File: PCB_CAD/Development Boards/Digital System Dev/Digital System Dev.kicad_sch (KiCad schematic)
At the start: 73 parts, among them J1 STLINK, J10 10V, J2 PINS_LEFT, J3 3V3, J4 5V, J5 GND, J6 PINS_LEFT, J7 DISP, J9 DC_IN, SW1 RESET, U1 STM32G474VETx, U2 DFR0570, U3 DFR0571, X1 HSE_24

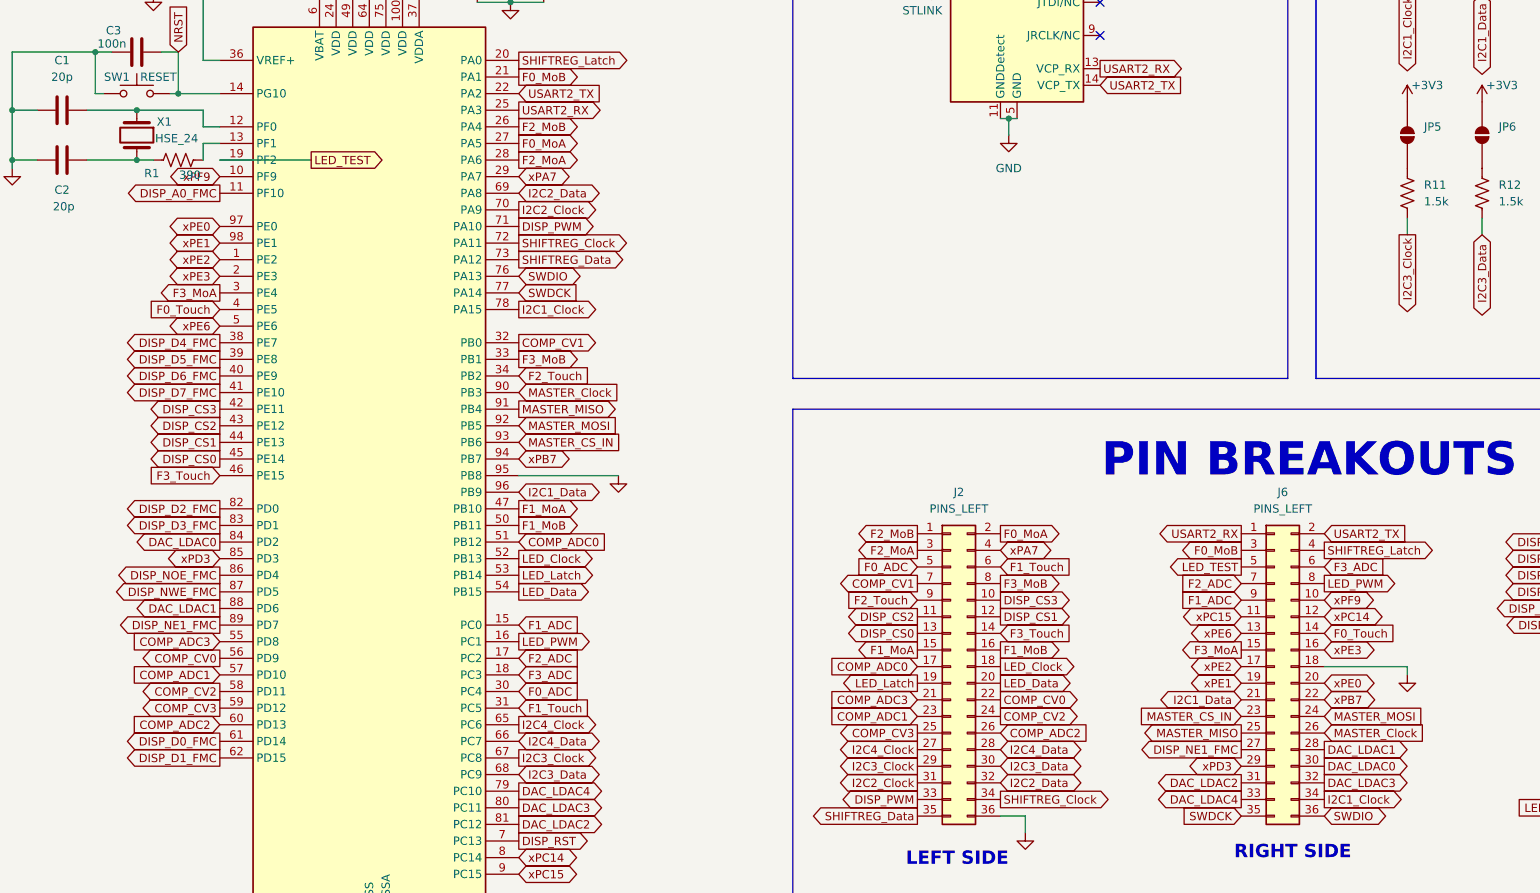
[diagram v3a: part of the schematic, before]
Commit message: fixed led flickering bug due to waiting for floating disconnnected i2c buses to respond until timeout
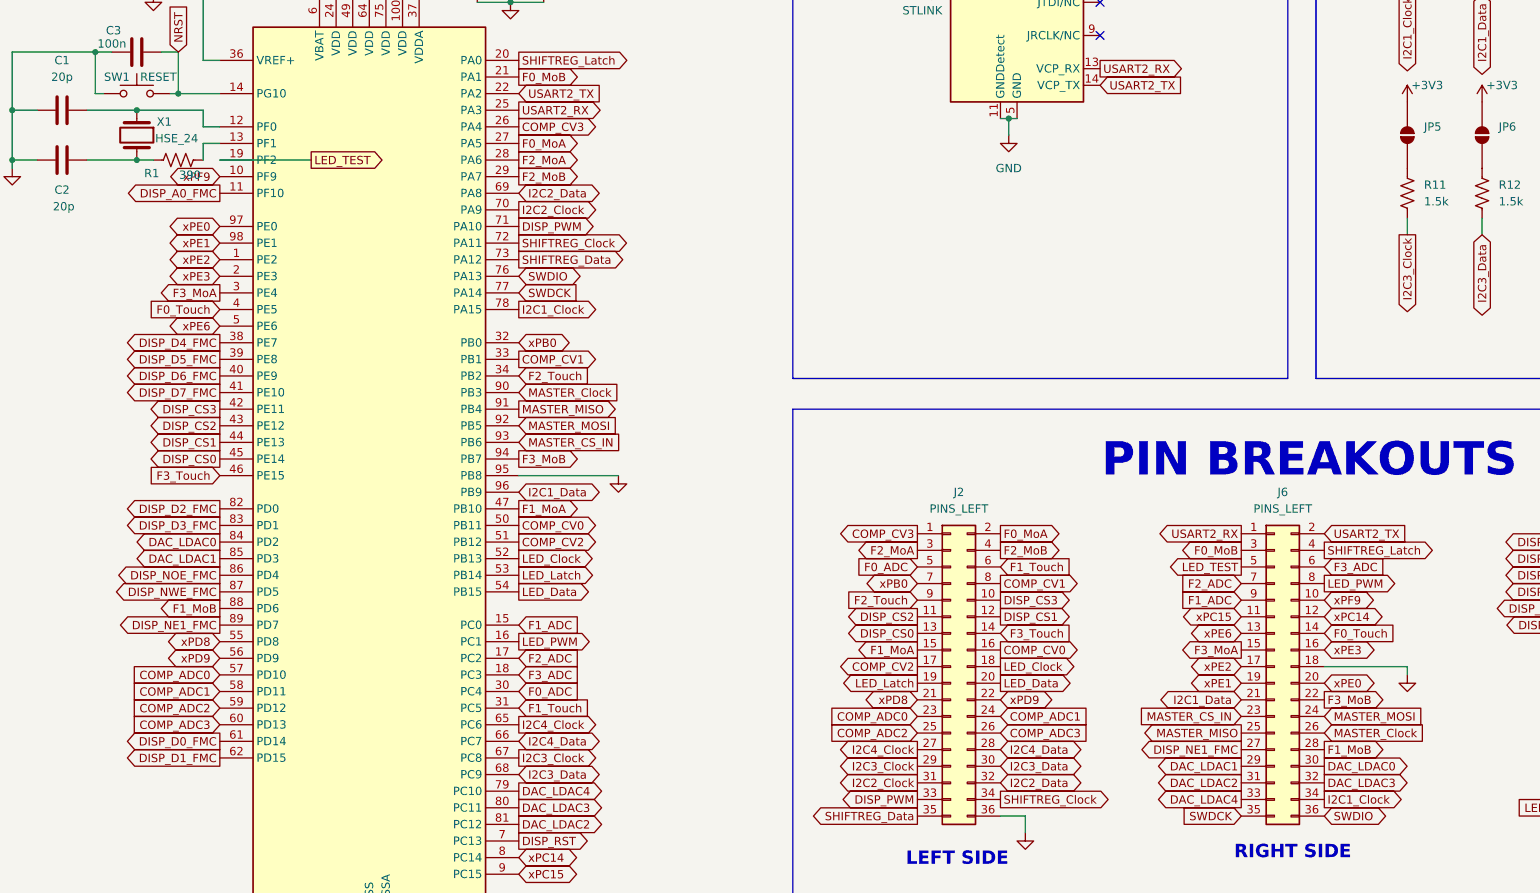
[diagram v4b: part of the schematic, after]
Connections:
- net xPA7 is gone; now on net F2_MoB: J2.4 (Pin_4), U1.29 (PA7)
- net xPB7 is gone; now on net F3_MoB: J6.22 (Pin_22), U1.94 (PB7)
- net xPD3 is gone; now on net DAC_LDAC1: J6.29 (Pin_29), U1.85 (PD3)
- net COMP_ADC0: now also J2.23 (Pin_23), U1.57 (PD10); no longer J2.17 (Pin_17), U1.51 (PB12)
- net COMP_ADC1: now also J2.24 (Pin_24), U1.58 (PD11); no longer J2.23 (Pin_23), U1.57 (PD10)
- net COMP_ADC2: now also J2.25 (Pin_25), U1.59 (PD12); no longer J2.26 (Pin_26), U1.60 (PD13)
- net COMP_ADC3: now also J2.26 (Pin_26), U1.60 (PD13); no longer J2.21 (Pin_21), U1.55 (PD8)
- net COMP_CV0: now also J2.16 (Pin_16), U1.50 (PB11); no longer J2.22 (Pin_22), U1.56 (PD9)
- net COMP_CV1: now also J2.8 (Pin_8), U1.33 (PB1); no longer J2.7 (Pin_7), U1.32 (PB0)
- net COMP_CV2: now also J2.17 (Pin_17), U1.51 (PB12); no longer J2.24 (Pin_24), U1.58 (PD11)
- net COMP_CV3: now also J2.1 (Pin_1), U1.26 (PA4); no longer J2.25 (Pin_25), U1.59 (PD12)
- net DAC_LDAC1: no longer J6.28 (Pin_28), U1.88 (PD6)
- net F1_MoB: now also J6.28 (Pin_28), U1.88 (PD6); no longer J2.16 (Pin_16), U1.50 (PB11)
- net F2_MoB: no longer J2.1 (Pin_1), U1.26 (PA4)
- net F3_MoB: no longer J2.8 (Pin_8), U1.33 (PB1)
- new net xPB0: J2.7 (Pin_7), U1.32 (PB0)
- new net xPD8: J2.21 (Pin_21), U1.55 (PD8)
- new net xPD9: J2.22 (Pin_22), U1.56 (PD9)

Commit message: fix num 2 for my cpu hungry i2c scheduler :c
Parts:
- removed C22, C29: 100n, Capacitor_SMD:C_0603_1608Metric, symbol Device:C
- removed D4, D5: 2N5062, Package_TO_SOT_THT:TO-92, symbol Device:Q_SCR_KGA
- removed DZ1: MMSZ5227B, Diode_SMD:D_SOD-123, symbol PCM_Diode_Zener_AKL:D_Zener_Generic
- removed DZ2: MMSZ5233BT1G, Diode_SMD:D_SOD-123, symbol PCM_Diode_Zener_AKL:D_Zener_Generic
- removed R15, R22: 1k, Resistor_SMD:R_0603_1608Metric, symbol Device:R_US
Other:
- note removed: "OVERVOLT PROTECTION"

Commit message: digilog dev board v1 finished and sent to jlc
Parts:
- D1, D2, D3: now in the parts list
- J6: value PINS_LEFT -> PINS_RIGHT
- R1: LCSC C497314 -> C4491
- R10, R11, R12, R13, R14, R7, R8, R9: LCSC (none) -> C22843
- R16, R23: LCSC C25822 -> C23228
- X1: LCSC C117881 -> C2253
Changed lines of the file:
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@@
 		(body_style 1)
 		(exclude_from_sim no)
-		(in_bom no)
+		(in_bom yes)
 		(on_board yes)
-		(in_pos_files no)
+		(in_pos_files yes)
 		(dnp no)
 		(property "Reference" "D3"
@@
 			)
 		)
+		(property "LCSC" "C22843"
+			(at 246.38 60.96 0)
+			(hide yes)
+			(show_name no)
+			(do_not_autoplace no)
+			(effects
+				(font
+					(size 1.27 1.27)
+				)
+			)
+		)
 		(pin "1"
 		)
@@
 			)
 		)
+		(property "LCSC" "C22843"
+			(at 271.78 97.79 0)
+			(hide yes)
+			(show_name no)
+			(do_not_autoplace no)
+			(effects
+				(font
+					(size 1.27 1.27)
+				)
+			)
+		)
 		(pin "1"
 		)
@@
 			)
 		)
+		(property "LCSC" "C22843"
+			(at 257.81 97.79 0)
+			(hide yes)
+			(show_name no)
+			(do_not_autoplace no)
+			(effects
+				(font
+					(size 1.27 1.27)
+				)
+			)
+		)
 		(pin "1"
 		)
@@
 			)
 		)
-		(property "LCSC" "C117881"
+		(property "LCSC" "C2253"
 			(at 52.07 88.9 90)
 			(hide yes)
@@
 			)
 		)
-		(property "LCSC" "C25822"
+		(property "LCSC" "C23228"
 			(at 349.25 200.66 90)
 			(hide yes)
@@
 			)
 		)
+		(property "LCSC" "C22843"
+			(at 257.81 60.96 0)
+			(hide yes)
+			(show_name no)
+			(do_not_autoplace no)
+			(effects
+				(font
+					(size 1.27 1.27)
+				)
+			)
+		)
 		(pin "1"
 		)
@@
 			)
 		)
-		(property "LCSC" "C25822"
+		(property "LCSC" "C23228"
 			(at 278.13 191.77 90)
 			(hide yes)
@@
 		(body_style 1)
 		(exclude_from_sim no)
-		(in_bom no)
+		(in_bom yes)
 		(on_board yes)
-		(in_pos_files no)
+		(in_pos_files yes)
 		(dnp no)
 		(property "Reference" "D1"
@@
 			)
 		)
+		(property "LCSC" "C22843"
+			(at 284.48 60.96 0)
+			(hide yes)
+			(show_name no)
+			(do_not_autoplace no)
+			(effects
+				(font
+					(size 1.27 1.27)
+				)
+			)
+		)
 		(pin "1"
 		)
@@
 			)
 		)
+		(property "LCSC" "C22843"
+			(at 273.05 60.96 0)
+			(hide yes)
+			(show_name no)
+			(do_not_autoplace no)
+			(effects
+				(font
+					(size 1.27 1.27)
+				)
+			)
+		)
 		(pin "1"
 		)
@@
 			)
 		)
+		(property "LCSC" "C22843"
+			(at 283.21 97.79 0)
+			(hide yes)
+			(show_name no)
+			(do_not_autoplace no)
+			(effects
+				(font
+					(size 1.27 1.27)
+				)
+			)
+		)
 		(pin "1"
 		)
@@
 		(body_style 1)
 		(exclude_from_sim no)
-		(in_bom no)
+		(in_bom yes)
 		(on_board yes)
-		(in_pos_files no)
+		(in_pos_files yes)
 		(dnp no)
 		(property "Reference" "D2"
@@
 			)
 		)
-		(property "Value" "PINS_LEFT"
+		(property "Value" "PINS_RIGHT"
 			(at 227.33 146.05 0)
 			(show_name no)
@@
 			)
 		)
-		(property "LCSC" "C497314"
+		(property "LCSC" "C4491"
 			(at 58.42 92.71 0)
 			(hide yes)
@@
 			(at 246.38 97.79 0)
 			(hide yes)
+			(show_name no)
+			(do_not_autoplace no)
+			(effects
+				(font
+					(size 1.27 1.27)
+				)
+			)
+		)
+		(property "LCSC" "C22843"
+			(at 246.38 97.79 0)
+			(hide yes)

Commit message: extreme pcb design
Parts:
- J2, J6: footprint Connector_PinHeader_2.54mm:PinHeader_2x18_P2.54mm_Vertical -> My Footprints:PinHeader_3x18_P2.54mm_Vertical_GND; symbol Connector_Generic:Conn_02x18_Odd_Even -> Connector_Generic_MountingPin:Conn_02x18_Odd_Even_MountingPin
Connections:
- net GND: now also J2.MP (MountPin), J6.MP (MountPin)
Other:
- moved on the sheet: D3, J7, R23
